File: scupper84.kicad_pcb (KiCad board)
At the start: 2 copper layers, 276.9 x 127.3 mm, 258 parts, among them K1 PG1350, K10 PG1350, K11 PG1350, K12 PG1350, K13 PG1350, K14 PG1350, K15 PG1350, K16 PG1350, K17 PG1350, K18 PG1350, K19 PG1350, K2 PG1350, K20 PG1350, K21 PG1350, K22 PG1350, K23 PG1350, K24 PG1350, K25 PG1350, K26 PG1350, K27 PG1350, K28 PG1350, K29 PG1350, K3 PG1350, K30 PG1350, K31 PG1350, K32 PG1350, K33 PG1350, K34 PG1350, K35 PG1350, K36 PG1350, K37 PG1350, K38 PG1350, K39 PG1350, K4 PG1350, K40 PG1350, K41 PG1350, K42 PG1350, K43 PG1350, K44 PG1350, K45 PG1350, K46 PG1350, K47 PG1350, K48 PG1350, K49 PG1350, K5 PG1350, K50 PG1350, K51 PG1350, K52 PG1350, K53 PG1350, K54 PG1350, K55 PG1350, K56 PG1350, K57 PG1350, K58 PG1350, K59 PG1350, K6 PG1350, K60 PG1350, K61 PG1350, K62 PG1350, K63 PG1350, K64 PG1350, K65 PG1350, K66 PG1350, K67 PG1350, K68 PG1350, K69 PG1350, K7 PG1350, K70 PG1350, K71 PG1350, K72 PG1350, K73 PG1350, K74 PG1350, K75 PG1350, K76 PG1350, K77 PG1350, K78 PG1350, K79 PG1350, K8 PG1350, K80 PG1350, K81 PG1350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

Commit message: Fiddling with routing a lot, trying the controller in the northwest corner.
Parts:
- moved U1 126.4 mm to (22.3, 23.3)
- moved SW1 98.7 mm to (34.9, 16.1)
- moved D73 68.3 mm to (227.0, -29.7)
- moved D57 52.9 mm to (248.7, -23.7)
- moved D80 52.9 mm to (252.7, -35.7)
- moved D10 52.9 mm to (189.5, -23.7)
- moved D11 52.9 mm to (195.4, -23.7)
- moved D12 52.9 mm to (201.3, -23.7)
- moved D13 52.9 mm to (207.3, -23.7)
- moved D14 52.9 mm to (213.2, -23.7)
- moved D15 52.9 mm to (219.1, -23.7)
- moved D24 52.9 mm to (185.6, -29.7)
- moved D25 52.9 mm to (191.5, -29.7)
- moved D26 52.9 mm to (197.4, -29.7)
- moved D27 52.9 mm to (203.3, -29.7)
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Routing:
- net Net-(D67-A): track 0.00 -> 268.3 mm, vias 0 -> 5
- net Net-(D78-A): track 0.00 -> 260.5 mm, vias 0 -> 1
- net Net-(D79-A): track 0.00 -> 232.6 mm, vias 0 -> 1
- net Net-(D68-A): track 0.00 -> 227.5 mm, vias 0 -> 5
- net Net-(D53-A): track 0.00 -> 224.0 mm, vias 0 -> 7
- net Net-(D80-A): track 0.00 -> 221.4 mm, vias 0 -> 1
- net Net-(D54-A): track 0.00 -> 220.2 mm, vias 0 -> 7
- net Net-(D69-A): track 0.00 -> 205.6 mm, vias 0 -> 5
- net Net-(D55-A): track 0.00 -> 198.1 mm, vias 0 -> 7
- net Net-(D70-A): track 0.00 -> 195.0 mm, vias 0 -> 3
- net Vcc: track 31.3 -> 218.8 mm, vias 2 -> 5
- net Net-(D56-A): track 0.00 -> 168.3 mm, vias 0 -> 7
- net Net-(D71-A): track 0.00 -> 165.4 mm, vias 0 -> 1
- net Net-(D73-A): track 0.00 -> 154.5 mm, vias 0 -> 1
- net Net-(D57-A): track 0.00 -> 149.0 mm, vias 0 -> 1
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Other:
- board size 276.9 x 127.3 mm -> 276.9 x 130.2 mm

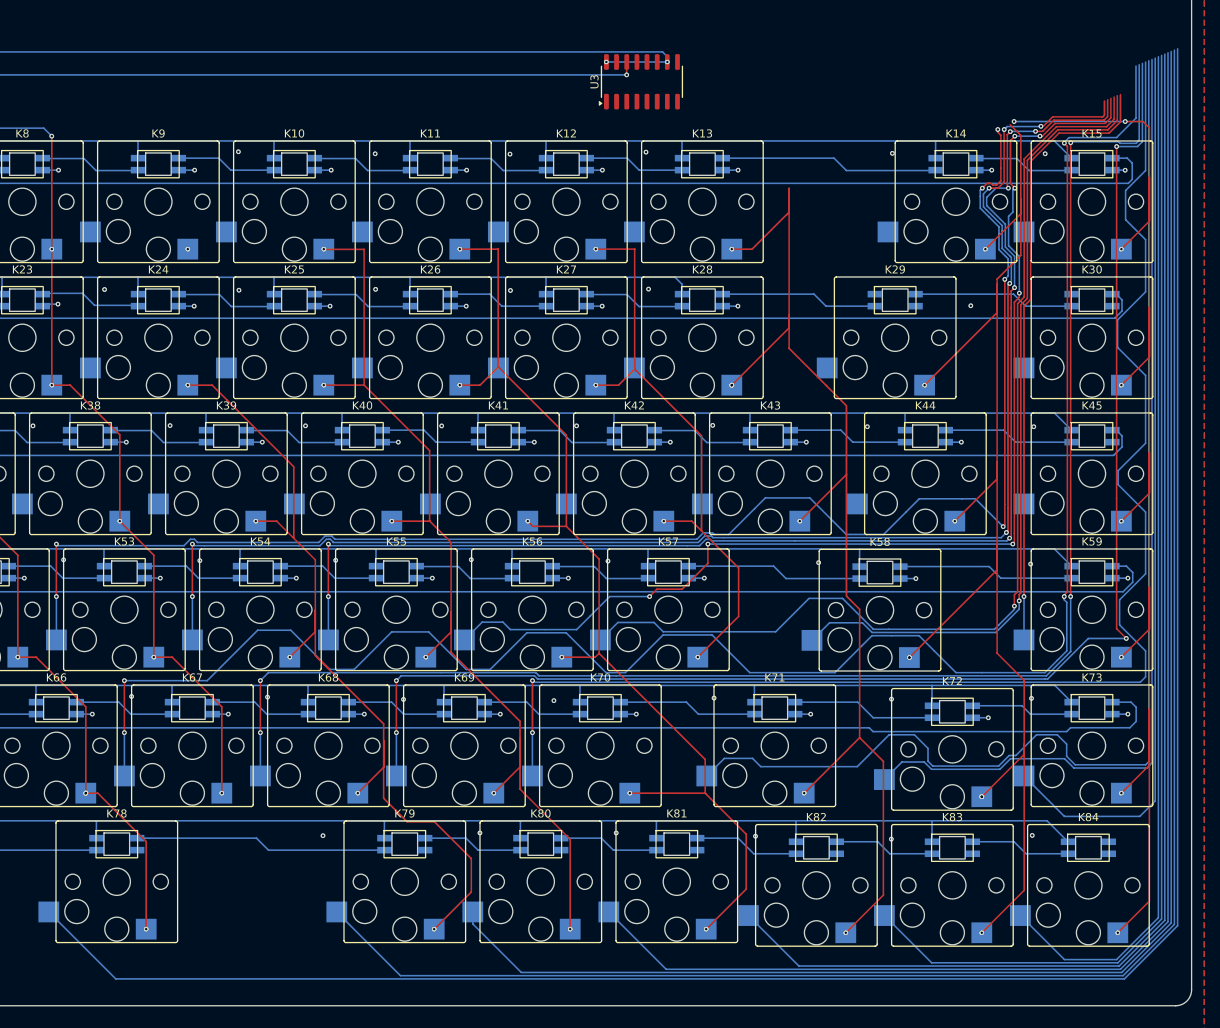
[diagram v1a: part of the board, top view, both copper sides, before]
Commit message: Trying a rule of vertical stuff on the front layer and horizontal stuff on the back layer.
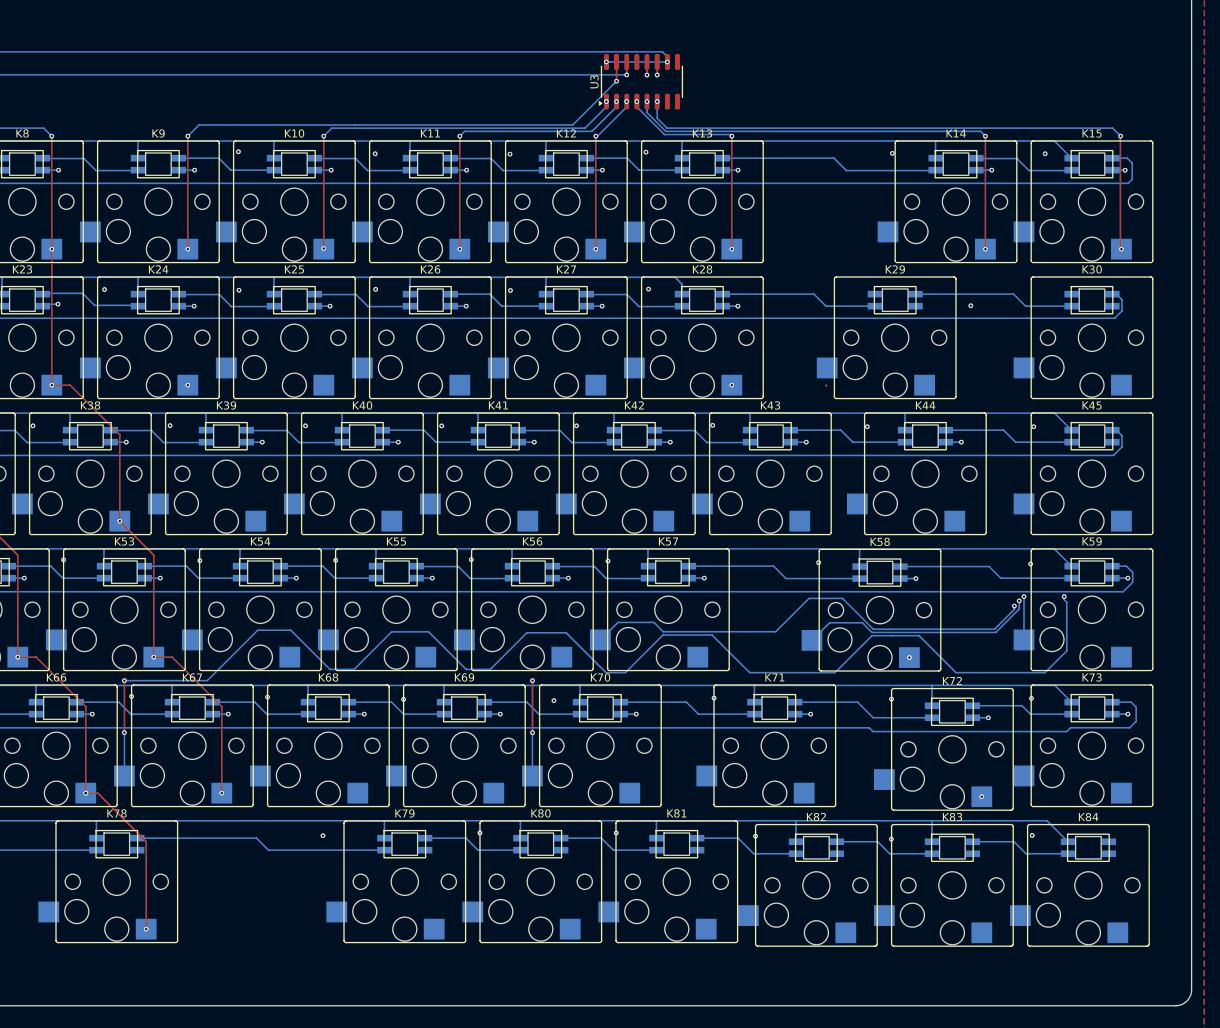
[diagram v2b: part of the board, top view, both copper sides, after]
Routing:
- net Net-(D78-A): track 260.5 -> 3.59 mm
- net Net-(D79-A): track 232.6 -> 12.6 mm
- net Net-(D80-A): track 221.4 -> 18.6 mm
- net Net-(D68-A): track 227.5 -> 30.6 mm, vias 5 -> 1
- net Net-(D53-A): track 224.0 -> 31.4 mm, vias 7 -> 1
- net Net-(D81-A): track 208.4 -> 24.5 mm
- net Net-(D54-A): track 220.2 -> 36.4 mm, vias 7 -> 0
- net Net-(D69-A): track 205.6 -> 24.6 mm, vias 5 -> 1
- net Net-(D55-A): track 198.1 -> 30.5 mm, vias 7 -> 0
- net Net-(D82-A): track 195.7 -> 30.4 mm
- net Net-(D70-A): track 195.0 -> 30.6 mm
- net Net-(D71-A): track 165.4 -> 12.8 mm
- net Net-(D83-A): track 183.6 -> 36.3 mm
- net Net-(D56-A): track 168.3 -> 24.5 mm, vias 7 -> 0
- net Net-(D84-A): track 171.6 -> 42.2 mm
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
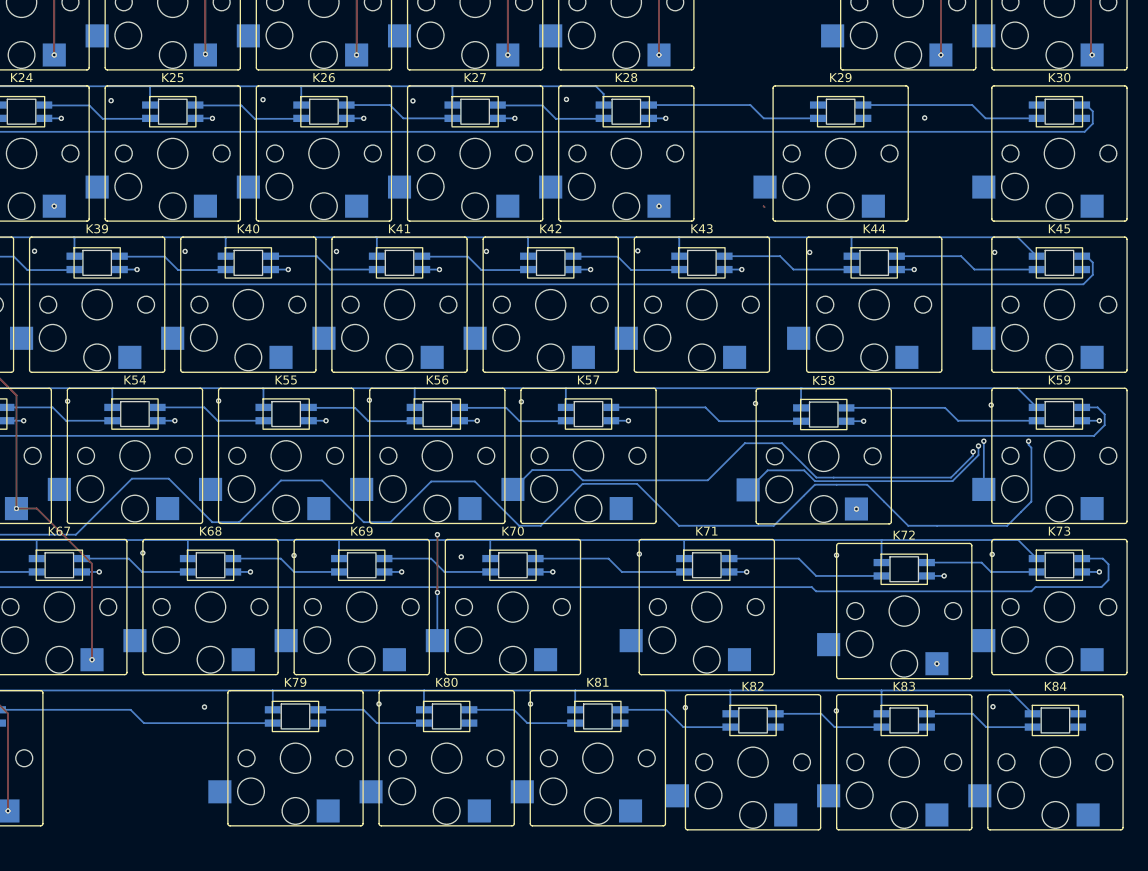
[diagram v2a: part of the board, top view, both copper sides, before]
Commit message: More rerouting.
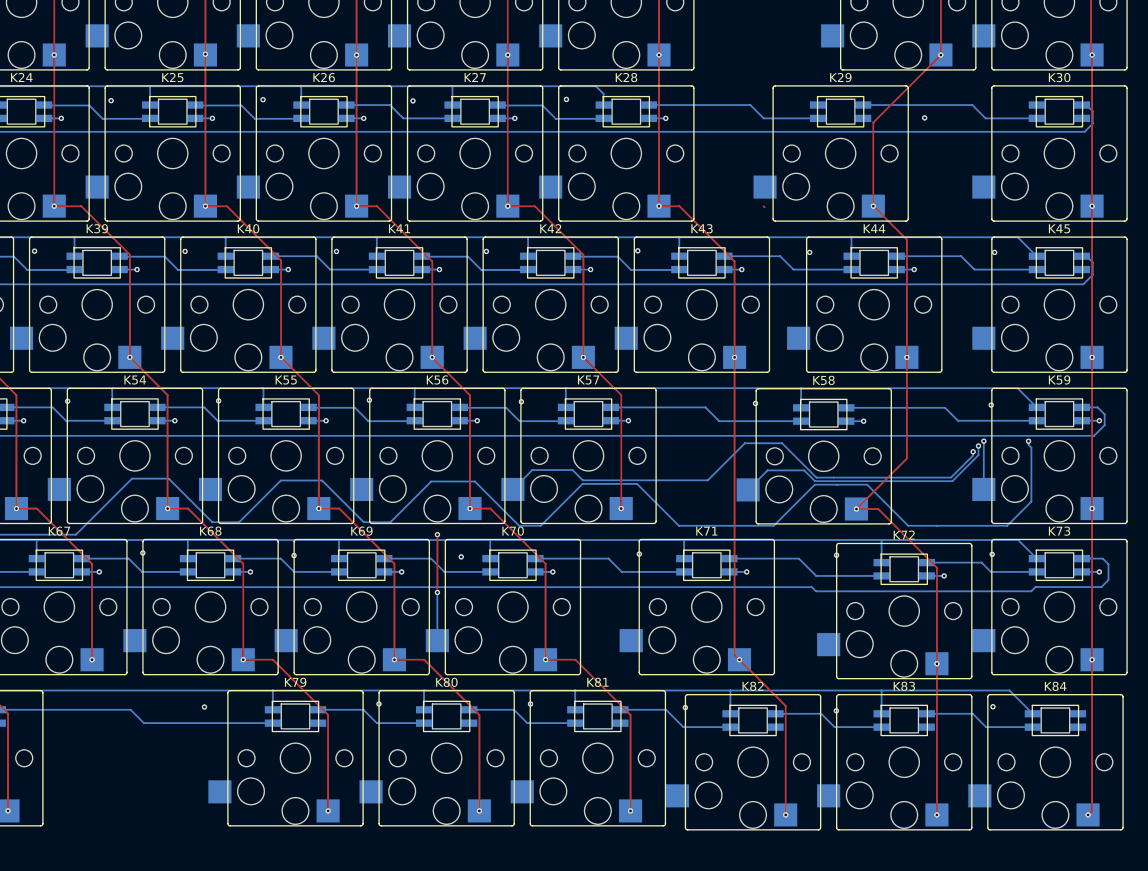
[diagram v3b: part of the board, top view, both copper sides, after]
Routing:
- net col8: track 73.0 -> 175.9 mm, vias 4 -> 8
- net col9: track 51.5 -> 154.1 mm, vias 3 -> 8
- net col10: track 35.9 -> 138.3 mm, vias 3 -> 8
- net col13: track 59.0 -> 156.7 mm, vias 5 -> 8
- net col12: track 28.3 -> 121.0 mm, vias 4 -> 7
- net col14: track 75.1 -> 161.3 mm, vias 3 -> 8
- net col11: track 20.2 -> 78.2 mm, vias 3 -> 6

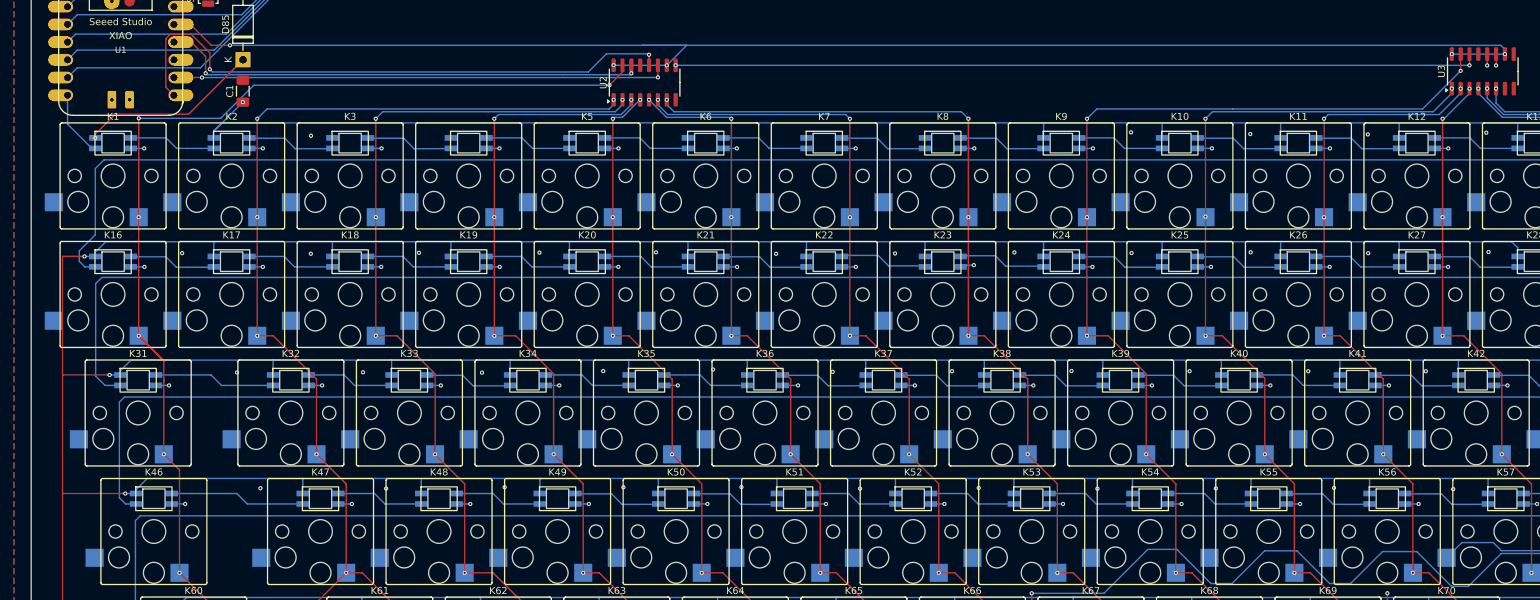
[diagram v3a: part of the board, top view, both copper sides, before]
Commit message: Starting the diode row-return routing.
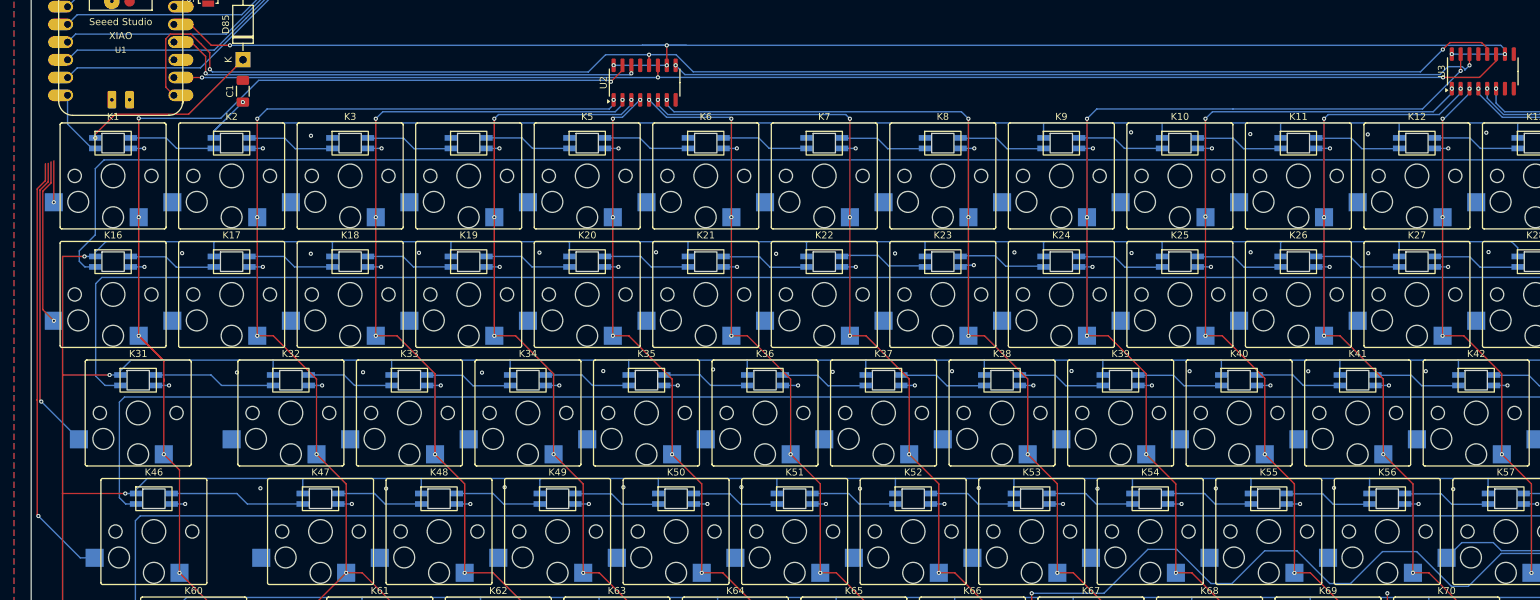
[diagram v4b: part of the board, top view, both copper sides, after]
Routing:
- net Net-(U1-D7): track 86.1 -> 208.5 mm
- net Net-(U1-SCK_D8): track 72.8 -> 193.3 mm
- net Net-(D46-A): track 0.00 -> 61.6 mm, vias 0 -> 1
- net Net-(D31-A): track 0.00 -> 42.4 mm, vias 0 -> 1
- net Net-(D16-A): track 0.00 -> 23.9 mm, vias 0 -> 1
- net Net-(D1-A): track 0.00 -> 5.96 mm, vias 0 -> 1
- net Net-(U2-QH'): track 115.5 -> 117.0 mm
- net Vcc: track 218.8 -> 217.6 mm, vias 5 -> 6

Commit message: Moving diodes to the back of the board.
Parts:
- D1, D10, D11, D12, D13, D14, D15, D16, D17, D18, D19, D2, D20, D21, D22, D23, D24, D25, D26, D27, D28, D29, D3, D30, D31, D32, D33, D34, D35, D36, D37, D38, D39, D4, D40, D41, D42, D43, D44, D45, D46, D47, D48, D49, D5, D50, D51, D52, D53, D54, D55, D56, D57, D58, D59, D6, D60, D61, D62, D63, D64, D65, D66, D67, D68, D69, D7, D70, D71, D72, D73, D74, D75, D76, D77, D78, D79, D8, D80, D81, D82, D83, D84, D9: moved to B.Cu
- moved D45 127.1 mm to (265.2, 84.2)
- moved D30 106.5 mm to (265.3, 67.2)
- moved D23 104.0 mm to (131.6, 67.2)
- moved D24 103.7 mm to (148.6, 67.2)
- moved D25 100.3 mm to (165.6, 67.2)
- moved D29 100.2 mm to (240.6, 67.2)
- moved D26 98.0 mm to (182.6, 67.2)
- moved D28 97.2 mm to (216.6, 67.2)
- moved D22 97.1 mm to (114.6, 67.2)
- moved D27 97.0 mm to (199.6, 67.2)
- moved D21 91.2 mm to (97.6, 67.2)
- moved D15 87.2 mm to (265.2, 50.2)
- moved D20 86.2 mm to (80.6, 67.2)
- moved D8 86.1 mm to (131.6, 50.2)
- moved D19 82.5 mm to (63.6, 67.2)
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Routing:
- net row1: track 95.6 -> 360.9 mm, vias 0 -> 2
- net row0: track 96.7 -> 344.3 mm, vias 0 -> 3
- net row3: track 171.6 -> 54.2 mm
- net row4: track 166.2 -> 54.0 mm
- net Net-(D61-A): track 0.00 -> 89.7 mm, vias 0 -> 1
- net row5: track 144.1 -> 54.8 mm
- net row2: track 120.2 -> 52.7 mm
- net Net-(D46-A): track 61.6 -> 0.00 mm, vias 1 -> 0
- net Net-(D31-A): track 42.4 -> 0.00 mm, vias 1 -> 0
- net Net-(D73-A): track 42.3 -> 0.00 mm, vias 1 -> 0
- net Net-(D84-A): track 42.2 -> 0.00 mm, vias 1 -> 0
- net Net-(D67-A): track 194.5 -> 158.0 mm, vias 4 -> 2
- net Net-(D54-A): track 36.4 -> 0.00 mm
- net Net-(D83-A): track 36.3 -> 0.00 mm, vias 1 -> 0
- net Net-(D53-A): track 31.4 -> 0.00 mm, vias 1 -> 0
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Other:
- board size 276.9 x 130.2 mm -> 278.9 x 130.2 mm
